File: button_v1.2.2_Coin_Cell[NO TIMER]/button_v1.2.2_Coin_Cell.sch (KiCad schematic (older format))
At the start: 18 parts, among them J1 Conn_01x05_Female, SW1 SW_Push, SW2 SW_Push, U1 TPS61097A, X1 ESP-12E

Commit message: :rocket: :full_moon_with_face:
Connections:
- net GND: now also SW1.2; no longer D1.1 (K)
- net RST: now also R6.2
- net VCC: now also D1.1 (K)
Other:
- moved on the sheet: D1, R6
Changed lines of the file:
@@
 L button_v1.2.2_Coin_Cell-rescue:LED-Device-button-timer-rescue-button-timer-v1.2-rescue-button-timer-v1.2-rescue-button-timer-v1.2.1_Coin_Cell-rescue D1
 U 1 1 602D28D1
-P 3950 3150
-F 0 "D1" V 3897 3228 50  0000 L CNN
-F 1 "LED" V 3988 3228 50  0000 L CNN
-F 2 "LED_SMD:LED_1206_3216Metric_Castellated" H 3950 3150 50  0001 C CNN
-F 3 "~" H 3950 3150 50  0001 C CNN
-	1    3950 3150
-	-1   0    0    1
-$EndComp
-Wire Wire Line
-	3800 2950 3800 3150
+P 2600 3400
+F 0 "D1" V 2547 3478 50  0000 L CNN
+F 1 "LED" V 2638 3478 50  0000 L CNN
+F 2 "LED_SMD:LED_1206_3216Metric_Castellated" H 2600 3400 50  0001 C CNN
+F 3 "~" H 2600 3400 50  0001 C CNN
+	1    2600 3400
+	0    -1   -1   0
+$EndComp
+Wire Wire Line
+	2800 3250 2600 3250
 $Comp
 L button_v1.2.2_Coin_Cell-rescue:R-Device-button-timer-rescue-button-timer-v1.2-rescue-button-timer-v1.2-rescue-button-timer-v1.2.1_Coin_Cell-rescue R6
 U 1 1 602D454A
-P 3650 2950
-F 0 "R6" H 3720 2996 50  0000 L CNN
-F 1 "1k" H 3720 2905 50  0000 L CNN
-F 2 "handsolder:R_0805_2012handsoldermod" V 3580 2950 50  0001 C CNN
-F 3 "~" H 3650 2950 50  0001 C CNN
-	1    3650 2950
-	0    1    1    0
-$EndComp
-Wire Wire Line
-	4100 3150 4250 3150
-Wire Wire Line
-	3500 2950 3350 2950
-Wire Wire Line
-	3350 2950 3350 2850
-Wire Wire Line
-	3350 2850 3250 2850
-Text Label 4250 3150 3    50   ~ 0
-GND
+P 2800 3100
+F 0 "R6" H 2870 3146 50  0000 L CNN
+F 1 "1k" H 2870 3055 50  0000 L CNN
+F 2 "handsolder:R_0805_2012handsoldermod" V 2730 3100 50  0001 C CNN
+F 3 "~" H 2800 3100 50  0001 C CNN
+	1    2800 3100
+	-1   0    0    1
+$EndComp
+Wire Wire Line
+	2600 3550 2600 3700
+Text Label 2600 3700 2    50   ~ 0
+VCC
 Connection ~ 2250 4150
 Wire Wire Line
@@
 Wire Wire Line
 	2700 4100 2800 4100
-Wire Wire Line
-	3250 2850 3250 2950
 Connection ~ 2900 4100
 Wire Wire Line
@@
 	2250 4150 2700 4150
 Wire Wire Line
-	2850 2950 2550 2950
+	2850 2950 2800 2950
 Text Label 2550 2950 2    50   ~ 0
 RST
+Connection ~ 2800 2950
+Wire Wire Line
+	2800 2950 2550 2950
+Text Label 3250 2950 0    50   ~ 0
+GND
 $EndSCHEMATC

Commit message: 3D Models etwas verbessert
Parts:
- J1: footprint Connector_PinHeader_2.54mm:PinHeader_1x05_P2.54mm_Vertical -> handsolder:PinSocket_1x05_P2.54mm_Vertical_mod
- SW1: footprint Button_Switch_THT:SW_PUSH_6mm -> handsolder:SW_PUSH_6mm_H8mm_mod
- SW2: footprint Button_Switch_SMD:SW_SPST_EVQPE1 -> handsolder:SW_SPST_B3U-1000P_mod
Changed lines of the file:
@@
 F 0 "SW1" H 3050 3235 50  0000 C CNN
 F 1 "SW_Push" H 3050 3144 50  0000 C CNN
-F 2 "Button_Switch_THT:SW_PUSH_6mm" H 3050 3150 50  0001 C CNN
+F 2 "handsolder:SW_PUSH_6mm_H8mm_mod" H 3050 3150 50  0001 C CNN
 F 3 "~" H 3050 3150 50  0001 C CNN
 	1    3050 2950
@@
 F 0 "J1" H 8328 3576 50  0000 L CNN
 F 1 "Conn_01x05_Female" H 8328 3485 50  0000 L CNN
-F 2 "Connector_PinHeader_2.54mm:PinHeader_1x05_P2.54mm_Vertical" H 8300 3550 50  0001 C CNN
+F 2 "handsolder:PinSocket_1x05_P2.54mm_Vertical_mod" H 8300 3550 50  0001 C CNN
 F 3 "~" H 8300 3550 50  0001 C CNN
 	1    8300 3550
@@
 F 0 "SW2" H 7800 2335 50  0000 C CNN
 F 1 "SW_Push" H 7800 2244 50  0000 C CNN
-F 2 "Button_Switch_SMD:SW_SPST_EVQPE1" H 7800 2250 50  0001 C CNN
+F 2 "handsolder:SW_SPST_B3U-1000P_mod" H 7800 2250 50  0001 C CNN
 F 3 "~" H 7800 2250 50  0001 C CNN
 	1    7800 2050

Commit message: cap between esp vcc and ground added
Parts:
- added C4: TAJB476M010TNJ, CAPPM3528X210N, symbol SamacSys_Parts:TAJB476M010TNJ
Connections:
- net GND: now also C4.2
- net VCC: now also C4.1
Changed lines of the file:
@@
 Text Label 3250 2950 0    50   ~ 0
 GND
+$Comp
+L SamacSys_Parts:TAJB476M010TNJ C4
+U 1 1 60363F43
+P 5300 3700
+F 0 "C4" V 5504 3830 50  0000 L CNN
+F 1 "TAJB476M010TNJ" V 5595 3830 50  0000 L CNN
+F 2 "CAPPM3528X210N" H 5650 3750 50  0001 L CNN
+F 3 "http://datasheets.avx.com/TAJ.pdf" H 5650 3650 50  0001 L CNN
+F 4 "Tantalum Capacitors - Solid SMD 10volts 47uF 20%" H 5650 3550 50  0001 L CNN "Description"
+F 5 "2.1" H 5650 3450 50  0001 L CNN "Height"
+F 6 "AVX" H 5650 3350 50  0001 L CNN "Manufacturer_Name"
+F 7 "TAJB476M010TNJ" H 5650 3250 50  0001 L CNN "Manufacturer_Part_Number"
+F 8 "581-TAJB476M010TNJ" H 5650 3150 50  0001 L CNN "Mouser Part Number"
+F 9 "https://www.mouser.co.uk/ProductDetail/AVX/TAJB476M010TNJ?qs=pYVYkI7xuRVorIKKgcxm0A%3D%3D" H 5650 3050 50  0001 L CNN "Mouser Price/Stock"
+F 10 "TAJB476M010TNJ" H 5650 2950 50  0001 L CNN "Arrow Part Number"
+F 11 "https://www.arrow.com/en/products/tajb476m010tnj/avx" H 5650 2850 50  0001 L CNN "Arrow Price/Stock"
+	1    5300 3700
+	0    1    1    0
+$EndComp
+Text Label 5300 4200 0    50   ~ 0
+GND
 $EndSCHEMATC

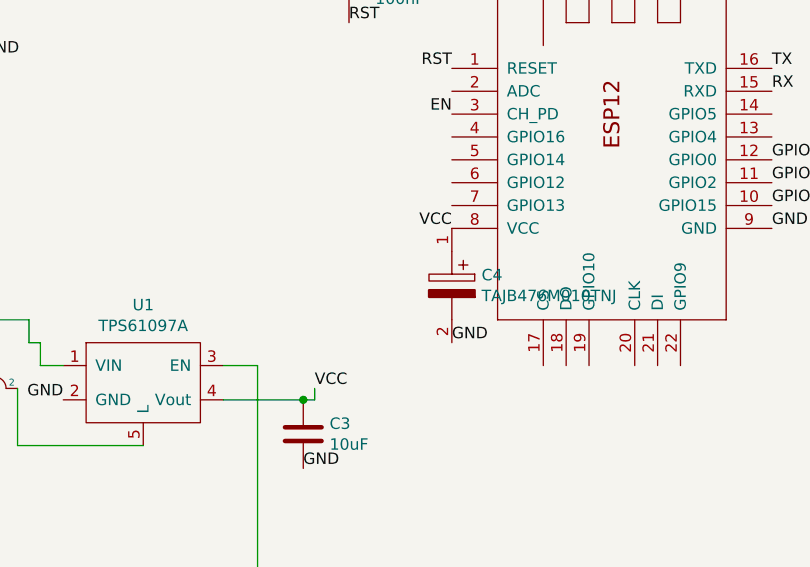
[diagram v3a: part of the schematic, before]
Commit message: Added 100nF decoupling capacitors between VCC and Ground of the ESP
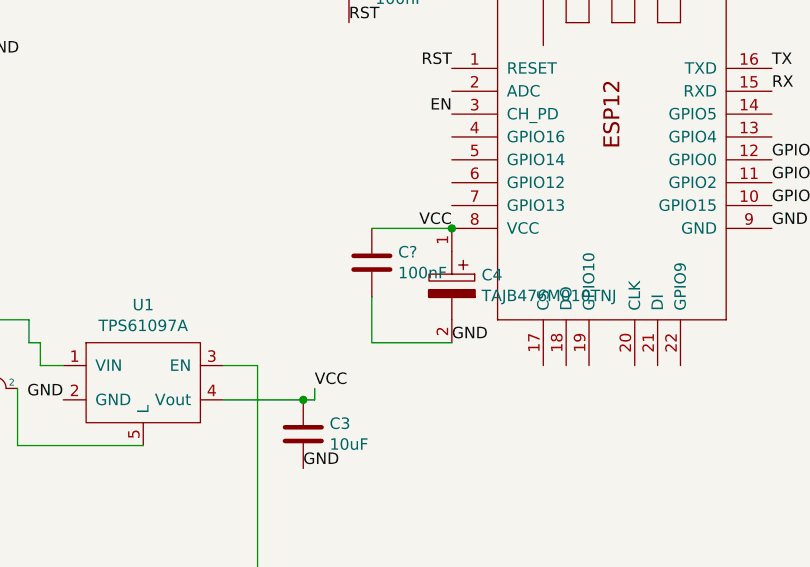
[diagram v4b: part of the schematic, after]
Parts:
- added C?: 100nF, handsolder:C_0402_1005Metric_Pad0.74x0.62mm_HandSoldermod, symbol Device:C
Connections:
- net GND: now also C?.2
- net VCC: now also C?.1
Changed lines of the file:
@@
 Text Label 5300 4200 0    50   ~ 0
 GND
+$Comp
+L Device:C C?
+U 1 1 60367A82
+P 4950 3850
+F 0 "C?" H 5065 3896 50  0000 L CNN
+F 1 "100nF" H 5065 3805 50  0000 L CNN
+F 2 "handsolder:C_0402_1005Metric_Pad0.74x0.62mm_HandSoldermod" H 4988 3700 50  0001 C CNN
+F 3 "~" H 4950 3850 50  0001 C CNN
+	1    4950 3850
+	1    0    0    -1
+$EndComp
+Wire Wire Line
+	4950 3700 5300 3700
+Connection ~ 5300 3700
+Wire Wire Line
+	4950 4000 4950 4200
+Wire Wire Line
+	4950 4200 5300 4200
 $EndSCHEMATC
